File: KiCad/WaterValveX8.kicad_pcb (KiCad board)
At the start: 2 copper layers, 66.7 x 42.3 mm, 89 parts, among them J10 Screw_Terminal_01x03, J2 Conn_01x03_Male, J3 Screw_Terminal_01x02, J4 Conn_01x01_Male, J5 Screw_Terminal_01x03, J6 Conn_01x04_Male, J7 Screw_Terminal_01x03, J8 Screw_Terminal_01x03, J9 Screw_Terminal_01x03, Q1 IRLML2502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

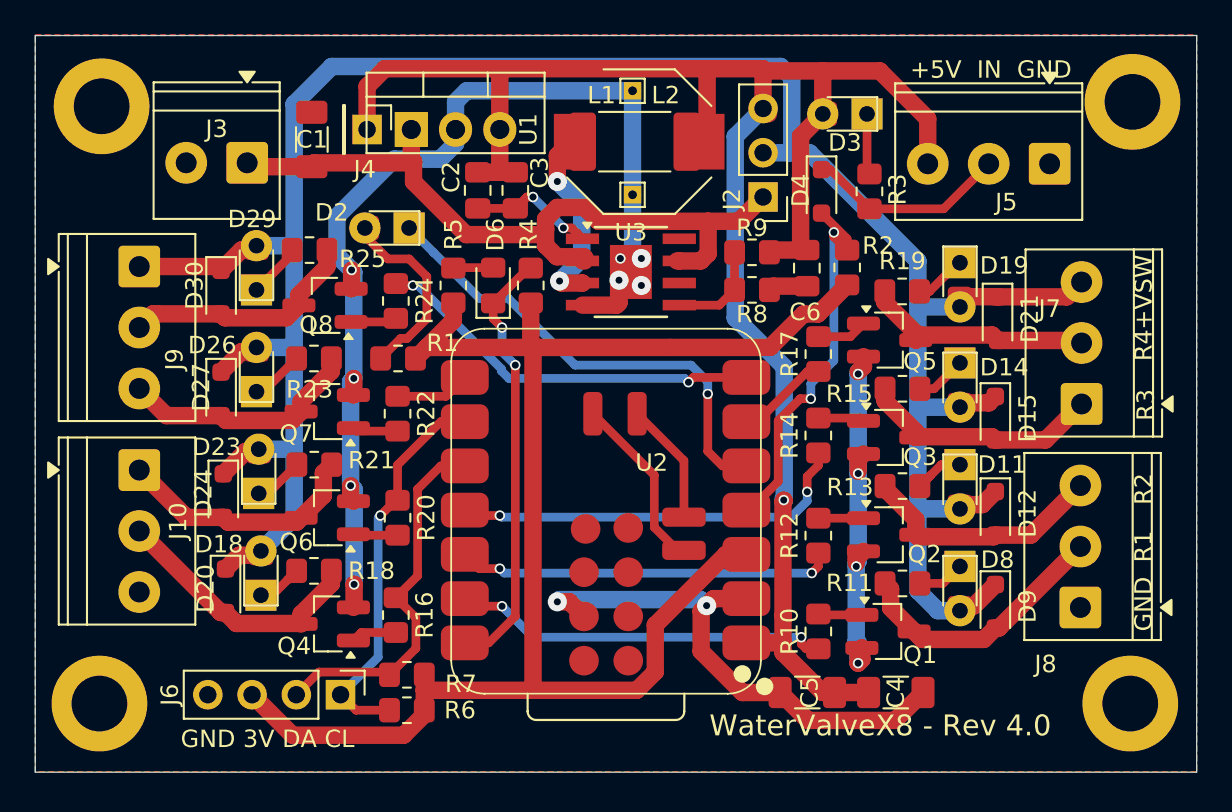
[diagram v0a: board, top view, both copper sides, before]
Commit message: Now a esp32c6 design only. To few usable ports on c3
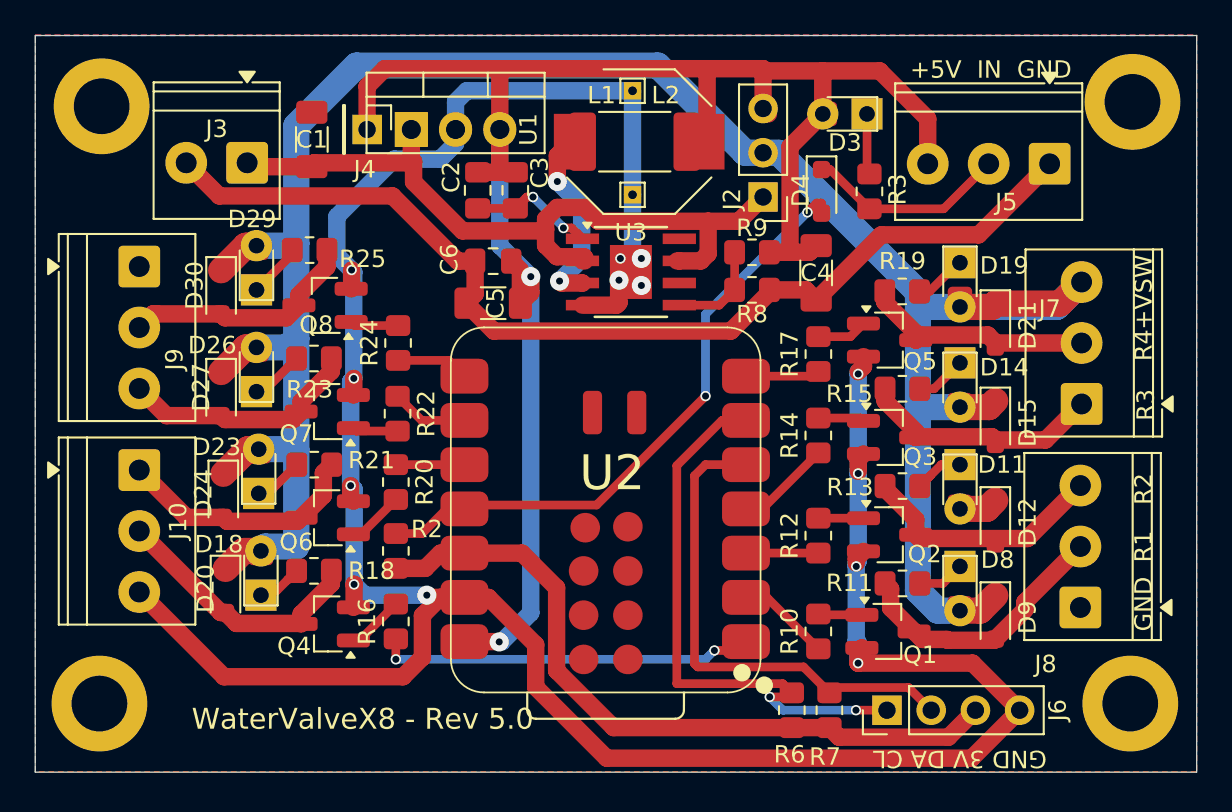
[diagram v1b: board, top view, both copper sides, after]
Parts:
- removed D1: LED, LED_THT:LED_D3.0mm
- removed D2, D6: LED, LED_SMD:LED_0805_2012Metric_Pad1.15x1.40mm_HandSolder
- removed R1, R5: 330, Resistor_SMD:R_0805_2012Metric_Pad1.20x1.40mm_HandSolder
- removed R4: 10k, Resistor_SMD:R_0805_2012Metric_Pad1.20x1.40mm_HandSolder
- D4: value D -> 1N4148SW
- L1: value L -> 22uH
- L2: value L -> 10uH
- R3: value 330 -> 430
- R8: value 88k7 -> 68k
- R9: value 20k -> 15k
- U2: footprint LOCAL1:XIAO-ESP32-C3C6-SMD -> LOCAL1:XIAO-ESP32-C6-SMD
- moved J6 31.4 mm to (184.8, 120.3), turned to 90 degrees
- moved R2 30.6 mm to (156.6, 111.1)
- moved C5 28.7 mm to (162.2, 96.9)
- moved C4 24.5 mm to (180.7, 95.2), turned to -90 degrees
- moved R7 24.3 mm to (181.5, 120.3), turned to 90 degrees
- moved R6 22.1 mm to (179.3, 120.3), turned to 90 degrees
- moved C6 18.0 mm to (162.2, 94.5), turned to 180 degrees
- moved R24 2.42 mm to (156.7, 99.2), turned to 90 degrees
- moved R20 2.05 mm to (156.6, 107.2)
- moved D9 0.64 mm to (191.0, 114.9)
- moved D12 0.51 mm to (191.0, 109.5)
- moved D21 0.40 mm to (191.0, 98.2)
- moved R16 0.36 mm to (156.6, 115.2), turned to 90 degrees
- moved D15 0.25 mm to (191.0, 103.8)
- moved U2 0.07 mm to (168.4, 108.7)
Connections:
- R10 pad 1: /D1 -> /Rel1
- R12 pad 1: /D2 -> /Rel2
- R14 pad 1: /D3 -> /Rel3
- R16 pad 1: /SDA -> /Rel5
- R17 pad 1: /D8 -> /Rel4
- R20 pad 1: /SCL -> /Rel6
- R22 pad 1: Net-(U2-GPIO17_D7_RX) -> /Rel7
- R24 pad 1: Net-(U2-GPIO16_D6_TX) -> /Rel8
- U2 pad 1: +5V -> /Rel5
- U2 pad 10: /SDA -> /Rel6
- U2 pad 11: /D3 -> /D10
- U2 pad 12: /D2 -> +3V3
- U2 pad 13: /D1 -> GND
- U2 pad 14: /GPIO2 -> +5V
- U2 pad 2: GND -> /Rel1
- U2 pad 20: GND -> unconnected-(U2-GND-Pad20)
- U2 pad 3: +3V3 -> /Rel2
- U2 pad 4: /D10 -> /Rel3
- U2 pad 5: Net-(D1-K) -> /SDA
- U2 pad 6: /D8 -> /SCL
- U2 pad 7: Net-(U2-GPIO16_D6_TX) -> /Rel4
- U2 pad 8: Net-(U2-GPIO17_D7_RX) -> /Rel8
- U2 pad 9: /SCL -> /Rel7
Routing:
- net GND: track 115.5 -> 222.0 mm, vias 14 -> 13
- net +3V3: track 90.4 -> 41.4 mm
- net Net-(D1-K): track 27.6 -> 0.00 mm, vias 1 -> 0
- net /GPIO2: track 25.7 -> 0.00 mm, vias 2 -> 0
- net /D3: track 23.6 -> 0.00 mm, vias 2 -> 0
- net Net-(U2-GPIO16_D6_TX): track 23.1 -> 0.00 mm, vias 2 -> 0
- net /D2: track 22.2 -> 0.00 mm, vias 2 -> 0
- net /D1: track 22.0 -> 0.00 mm, vias 2 -> 0
- net /Rel5: track 0.00 -> 21.7 mm, vias 0 -> 2
- net /D10: track 22.7 -> 35.6 mm
- net Net-(D1-A): track 11.1 -> 0.00 mm
- net unconnected-(U2-GND-Pad16): track 10.2 -> 0.00 mm
- net /SCL: track 22.8 -> 32.8 mm, vias 1 -> 2
- net /SDA: track 21.5 -> 29.0 mm
- net unconnected-(U2-BAT-Pad15): track 7.05 -> 0.00 mm
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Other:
- board text added: "WaterValveX8 - Rev 5.0"
- board text removed: "WaterValveX8 - Rev 4.0"

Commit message: Moved power in to top right
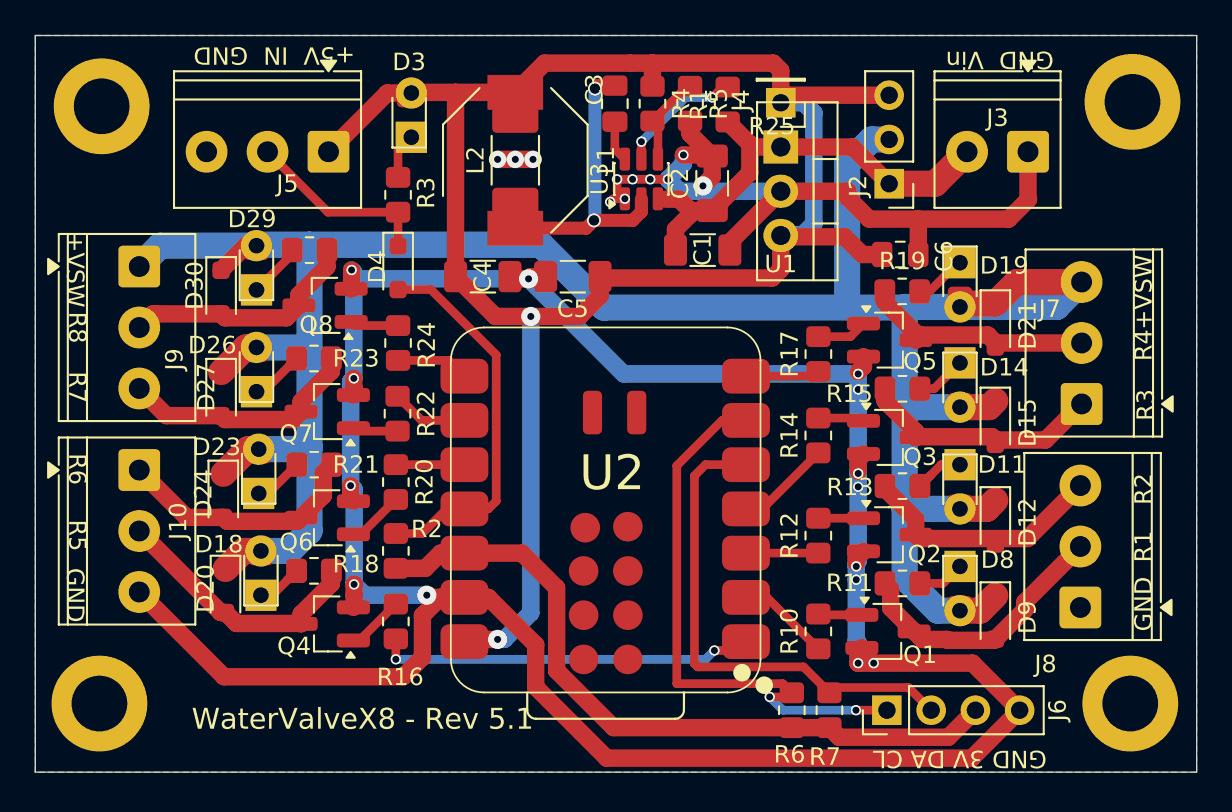
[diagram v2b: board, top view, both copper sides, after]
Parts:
- removed R8: 68k, Resistor_SMD:R_0805_2012Metric_Pad1.20x1.40mm_HandSolder
- removed R9: 15k, Resistor_SMD:R_0805_2012Metric_Pad1.20x1.40mm_HandSolder
- removed TP1, TP2: TestPoint, TestPoint:TestPoint_THTPad_1.0x1.0mm_Drill0.5mm
- added R1: 10k, Resistor_SMD:R_0805_2012Metric_Pad1.20x1.40mm_HandSolder, F.Cu at (175.6, 85.5)
- added R4: 68k, Resistor_SMD:R_0805_2012Metric_Pad1.20x1.40mm_HandSolder, F.Cu at (171.3, 85.4)
- added R5: 12k, Resistor_SMD:R_0805_2012Metric_Pad1.20x1.40mm_HandSolder, F.Cu at (173.5, 85.4)
- C2: value 100nF -> 22uF; footprint Capacitor_SMD:C_0805_2012Metric_Pad1.18x1.45mm_HandSolder -> Capacitor_SMD:C_1206_3216Metric_Pad1.33x1.80mm_HandSolder
- C3: value 22nF -> 100nF
- L1: value 22uH -> 10uH
- L2: value 10uH -> 4.7uH; footprint Inductor_SMD:L_2512_6332Metric_Pad1.52x3.35mm_HandSolder -> Inductor_SMD:L_2010_5025Metric_Pad1.52x2.65mm_HandSolder
- U3: value MT2499A -> TPS561201/08 or TPS563200; footprint Package_SO:TI_SO-PowerPAD-8 -> Package_TO_SOT_SMD:SOT-23-6
- moved J3 44.8 mm to (192.9, 88.2)
- moved J5 41.4 mm to (152.7, 88.2)
- moved R3 27.1 mm to (156.7, 90.7)
- moved D5 26.2 mm to (157.5, 87.4), turned to 90 degrees
- moved D3 25.0 mm to (157.4, 86.1), turned to 90 degrees
- moved D4 24.7 mm to (156.7, 94.9)
- moved J4 23.8 mm to (178.7, 85.4), turned to 180 degrees
- moved C6 23.4 mm to (185.5, 94.1), turned to 0 degrees
- moved C1 23.3 mm to (174.2, 93.9), turned to 0 degrees
- moved U1 21.2 mm to (178.7, 87.9), turned to -90 degrees
- moved C4 19.1 mm to (161.6, 95.4), turned to 0 degrees
- moved C2 13.5 mm to (174.8, 90.0)
- moved C3 7.58 mm to (169.2, 85.4)
- moved J2 7.28 mm to (184.9, 90.0)
- moved L1 7.19 mm to (163.4, 88.7), turned to 90 degrees
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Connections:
- C2 pad 1: Net-(U3-BS) -> /Vin
- C2 pad 2: +5V -> GND
- C3 pad 1: Net-(U3-BS) -> Net-(U3-VBST)
- C3 pad 2: +5V -> /IND1
- J3 pad 1: /Vin -> GND
- J3 pad 2: GND -> /Vin
- J5 pad 1: GND -> +5V
- J5 pad 3: +5V -> GND
- U3 pad 1: Net-(U3-BS) -> GND
- U3 pad 2: /Vin -> /IND1
- U3 pad 3: /IND1 -> /Vin
- U3 pad 4: GND -> Net-(U3-VFB)
- U3 pad 6: unconnected-(U3-NC-Pad6) -> Net-(U3-VBST)
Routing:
- net /Vin: track 44.4 -> 26.2 mm
- net GND: track 222.0 -> 203.8 mm, vias 13 -> 25
- net /D10: track 35.6 -> 22.1 mm, vias 2 -> 0
- net +VSW: track 133.1 -> 144.4 mm
- net Net-(U3-BS): track 7.74 -> 0.00 mm, vias 2 -> 0
- net /IND1: track 11.5 -> 17.2 mm
- net Net-(U3-VFB): track 0.00 -> 5.30 mm
- net +5V: track 107.0 -> 110.3 mm
- net Net-(U3-VBST): track 0.00 -> 2.39 mm
- net Net-(U3-EN): track 5.70 -> 7.26 mm, vias 0 -> 2
- net Net-(D3-K): track 3.75 -> 2.62 mm
- net Net-(D4-K): track 11.6 -> 10.9 mm
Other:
- rule pad_to_mask_clearance: 0.051 -> 0
- board text added: "(C) 2026 Hans Rune Bue <email@hansrune.net>"
- board text added: "GND Vin"
- board text added: "R5"
- board text added: "R6"
- board text added: "R7"
- board text added: "R8"
- board text added: "WaterValveX8 - Rev 5.1"
- board text removed: "(C) 2025 Hans Rune Bue <email@hansrune.net>"
- board text removed: "WaterValveX8 - Rev 5.0"
